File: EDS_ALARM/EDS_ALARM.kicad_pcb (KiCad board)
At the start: 2 copper layers, 3 parts, among them U1 STM32F411RETx, U2 CMWX1ZZABZ-078

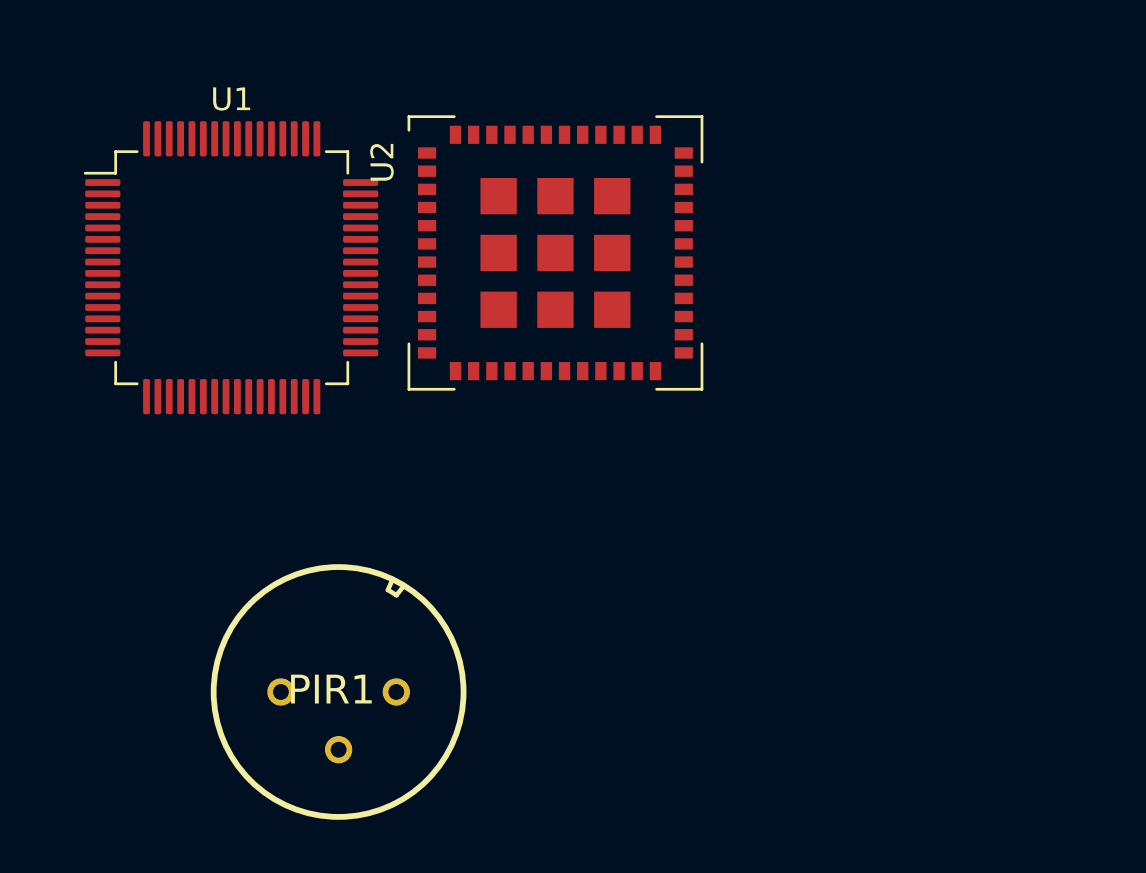
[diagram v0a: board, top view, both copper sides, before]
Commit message: Adding correct footprints to corresponding symbols, adding cristal
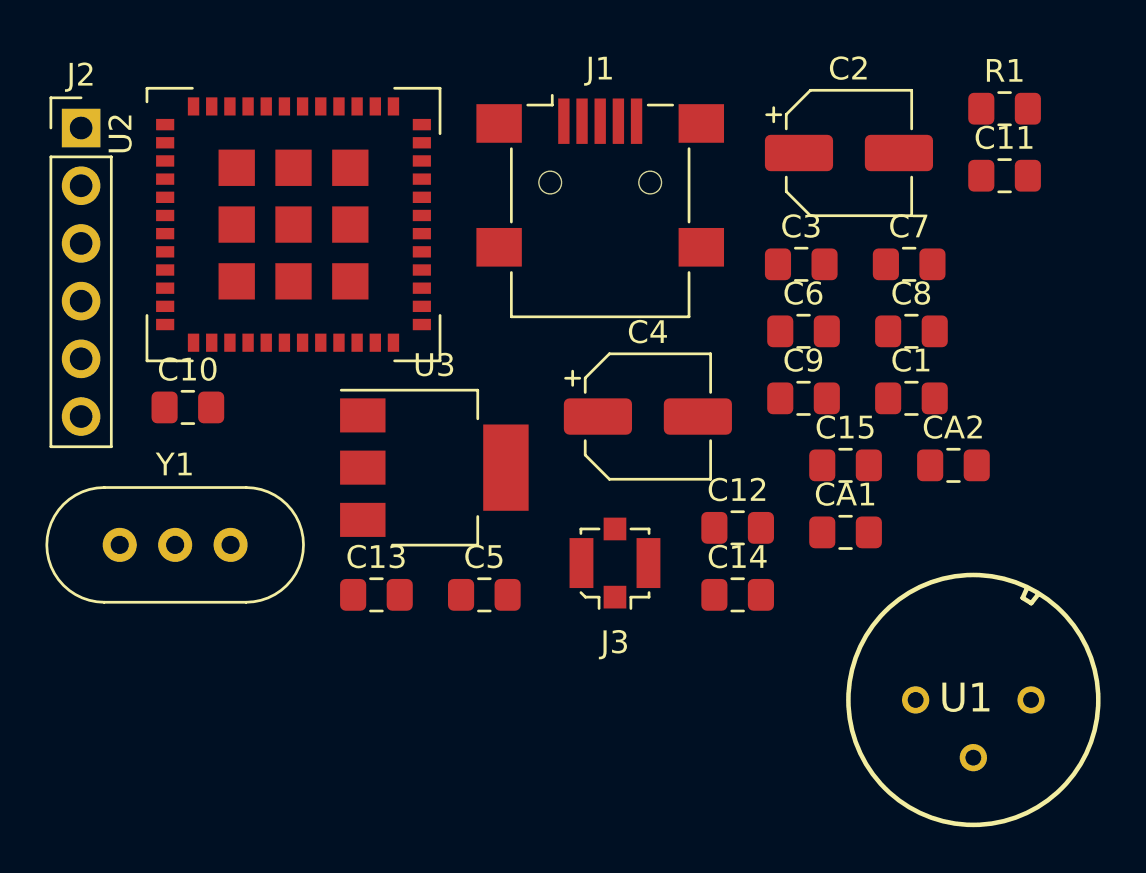
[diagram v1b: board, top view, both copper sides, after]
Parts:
- removed PIR1: EKMC1601111, VZ-STANDARD
- added C1: 100n, Capacitor_SMD:C_0805_2012Metric_Pad1.15x1.40mm_HandSolder, F.Cu at (175.1, 69.6)
- added C10: 100n, Capacitor_SMD:C_0805_2012Metric_Pad1.15x1.40mm_HandSolder, F.Cu at (143.2, 70.0)
- added C11: 1u, Capacitor_SMD:C_0805_2012Metric_Pad1.15x1.40mm_HandSolder, F.Cu at (179.2, 59.8)
- added C12: 100n, Capacitor_SMD:C_0805_2012Metric_Pad1.15x1.40mm_HandSolder, F.Cu at (167.4, 75.3)
- added C13: 100N, Capacitor_SMD:C_0805_2012Metric_Pad1.15x1.40mm_HandSolder, F.Cu at (151.5, 78.3)
- added C14: 18p, Capacitor_SMD:C_0805_2012Metric_Pad1.15x1.40mm_HandSolder, F.Cu at (167.4, 78.3)
- added C15: 18p, Capacitor_SMD:C_0805_2012Metric_Pad1.15x1.40mm_HandSolder, F.Cu at (172.2, 72.6)
- added C2: 10µ, Capacitor_SMD:CP_Elec_5x4.4, F.Cu at (172.3, 58.8)
- added C3: 100n, Capacitor_SMD:C_0805_2012Metric_Pad1.15x1.40mm_HandSolder, F.Cu at (170.2, 63.7)
- added C4: 10µ, Capacitor_SMD:CP_Elec_5x4.4, F.Cu at (163.5, 70.4)
- added C5: 100n, Capacitor_SMD:C_0805_2012Metric_Pad1.15x1.40mm_HandSolder, F.Cu at (156.3, 78.3)
- added C6: 10µ, Capacitor_SMD:C_0805_2012Metric_Pad1.15x1.40mm_HandSolder, F.Cu at (170.3, 66.7)
- added C7: 100n, Capacitor_SMD:C_0805_2012Metric_Pad1.15x1.40mm_HandSolder, F.Cu at (175.0, 63.7)
- added C8: 100n, Capacitor_SMD:C_0805_2012Metric_Pad1.15x1.40mm_HandSolder, F.Cu at (175.1, 66.7)
- added C9: 100n, Capacitor_SMD:C_0805_2012Metric_Pad1.15x1.40mm_HandSolder, F.Cu at (170.3, 69.6)
- added CA1: 1µ, Capacitor_SMD:C_0805_2012Metric_Pad1.15x1.40mm_HandSolder, F.Cu at (172.2, 75.5)
- added CA2: 1µ, Capacitor_SMD:C_0805_2012Metric_Pad1.15x1.40mm_HandSolder, F.Cu at (176.9, 72.6)
- added J1: USB_B_Micro, Connector_USB:USB_Mini-B_Lumberg_2486_01_Horizontal, F.Cu at (161.4, 60.1)
- added J2: Conn_01x06_Male, Connector_PinHeader_2.54mm:PinHeader_1x06_P2.54mm_Vertical, F.Cu at (138.5, 57.7)
- added J3: 73412-0110, Connector_Coaxial:U.FL_Molex_MCRF_73412-0110_Vertical, F.Cu at (162.0, 76.9)
- added R1: 10k, Resistor_SMD:R_0805_2012Metric_Pad1.15x1.40mm_HandSolder, F.Cu at (179.2, 56.9)
- added U3: LT1117-3.3, Package_TO_SOT_SMD:SOT-223, F.Cu at (154.1, 72.7)
- added Y1: 8.0MHz, Crystal:Crystal_HC49-U-3Pin_Vertical, F.Cu at (140.2, 76.1)
- U1: value STM32F411RETx -> EKMC1601111; footprint Package_QFP:LQFP-64_10x10mm_P0.5mm -> EKMC1601111:VZ-STANDARD
- moved U1 37.8 mm to (177.8, 82.9)
- moved U2 11.6 mm to (147.9, 62.0)
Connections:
- net Net-(U2-Pad22) renamed /DAC1
- net Net-(U2-Pad23) renamed /SmokeSensor
- U1 pad 2: Net-(U1-Pad2) -> /ADC2
- U1 pad 3: Net-(U1-Pad3) -> GND
- U2 pad 24: Net-(U2-Pad24) -> /ADC2
- U2 pad 32: Net-(U2-Pad32) -> +3V3
- U2 pad 34: Net-(U2-Pad34) -> /NRST
- U2 pad 4: Net-(U2-Pad4) -> +3V3
- U2 pad 41: Net-(U2-Pad41) -> /SWDIO
- U2 pad 42: Net-(U2-Pad42) -> /SWCLK
- U2 pad 48: Net-(U2-Pad48) -> +3V3
- U2 pad 5: Net-(U2-Pad5) -> +3V3
- U2 pad 6: Net-(U2-Pad6) -> +3V3

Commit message: Finished layout
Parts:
- removed C14, C15: 18p, Capacitor_SMD:C_0805_2012Metric_Pad1.15x1.40mm_HandSolder
- removed Y1: 8.0MHz, Crystal:Crystal_HC49-U-3Pin_Vertical
- added D1: LED, LED_SMD:LED_0805_2012Metric, F.Cu at (184.2, 94.0)
- added D2: LED, LED_SMD:LED_0805_2012Metric, F.Cu at (190.5, 94.1)
- added RV1: 23BR1KLFTR, 23BR1KLFTR:23B_1, F.Cu at (204.5, 99.1)
- added SW1: SW_Push, Button_Switch_SMD:SW_SPST_PTS645, F.Cu at (218.1, 82.7)
- added U4: TGS2611-E00, TGS2611-E00:TGS2611C00, F.Cu at (207.0, 111.8)
- added kmtg1603: Buzzer, KMTG1603-1:KMTG16031, F.Cu at (221.0, 104.1)
- moved J2 91.0 mm to (227.3, 77.5)
- moved J1 60.3 mm to (193.0, 111.5)
- moved C12 53.2 mm to (218.4, 90.3), turned to 180 degrees
- moved C13 50.6 mm to (199.6, 94.0), turned to 180 degrees
- moved C2 48.1 mm to (191.8, 102.9)
- moved J3 47.3 mm to (207.0, 91.4)
- moved C3 47.0 mm to (198.1, 101.6), turned to 270 degrees
- moved U3 46.9 mm to (182.6, 109.9), turned to 90 degrees
- moved U2 46.3 mm to (188.0, 85.1)
- moved C10 42.8 mm to (177.8, 95.2)
- moved C5 34.9 mm to (176.5, 106.7), turned to 180 degrees
- moved C4 34.5 mm to (178.1, 101.6)
- moved C1 33.6 mm to (185.4, 101.6), turned to 270 degrees
- moved C11 31.6 mm to (198.1, 85.1), turned to 270 degrees
- moved CA2 30.6 mm to (201.9, 90.2), turned to 90 degrees
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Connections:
- U2 pad 20: Net-(U2-Pad20) -> /LED2
- U2 pad 23: /SmokeSensor -> /ADC3
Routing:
- net +3V3: track 0.00 -> 114.4 mm, vias 0 -> 2
- net /NRST: track 0.00 -> 50.0 mm
- net +5V: track 0.00 -> 48.6 mm
- net /SWDIO: track 0.00 -> 47.7 mm
- net /SWCLK: track 0.00 -> 47.3 mm
- net /DAC1: track 0.00 -> 42.8 mm
- net /ADC2: track 0.00 -> 23.9 mm
- net /ADC3: track 0.00 -> 14.1 mm
- net Net-(RV1-Pad1): track 0.00 -> 12.2 mm
- net Net-(R1-Pad1): track 0.00 -> 9.42 mm
- net Net-(C13-Pad1): track 0.00 -> 8.87 mm
- net Net-(C13-Pad2): track 0.00 -> 8.54 mm
- net GND: track 0.00 -> 8.41 mm
- net /LED2: track 0.00 -> 4.76 mm
- added copper zone on B.Cu, net GND
- added copper zone on F.Cu, net GND
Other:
- board outline added: 58.4 x 41.9 mm
- net class Default: trace_width 0.25 -> 0.1
- net class Power added: clearance 0.2, trace_width 0.25, via_dia 0.8, via_drill 0.4
- rule solder_mask_min_width: 0.25 -> 0.1
- rule trace_min: 0.2 -> 0.1
- board text added: "Alfredo Martinez Hernandez"
- board text added: "INFO"
- board text added: "Jean Dumoulin"
- board text added: "POWER"

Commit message: Last layout modifications
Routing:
- net /NRST: track 50.0 -> 69.8 mm
- net /SWDIO: track 47.7 -> 66.3 mm
- net GND: track 8.41 -> 18.4 mm
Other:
- net class Default: trace_width 0.1 -> 0.2
- net class Power: trace_width 0.25 -> 0.35

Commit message: Layout improve
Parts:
- moved R1 8.01 mm to (188.6, 77.0)
- moved C2 1.27 mm to (191.8, 101.6), turned to 90 degrees
- moved C7 1.27 mm to (177.8, 78.7), turned to 180 degrees
- moved C10 1.27 mm to (177.8, 94.0), turned to 180 degrees
- moved C6 1.27 mm to (177.8, 82.5), turned to 180 degrees
- moved C8 1.27 mm to (177.8, 86.4), turned to 180 degrees
- moved C9 1.27 mm to (177.8, 90.2), turned to 180 degrees
- moved D2 0.13 mm to (190.5, 94.0), turned to 180 degrees
- turned C1 to 90 degrees
- turned C3 to 90 degrees
- turned D1 to 180 degrees
- turned U1 to 270 degrees
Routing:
- net +3V3: track 114.6 -> 128.6 mm, vias 2 -> 0
- net +5V: track 48.6 -> 41.6 mm
- net Net-(R1-Pad1): track 9.48 -> 2.94 mm
- net /SWCLK: track 47.2 -> 42.7 mm
- net /ADC2: track 23.9 -> 25.7 mm
- net GND: track 18.4 -> 17.4 mm, vias 0 -> 1
- net /LED2: track 4.76 -> 3.86 mm
